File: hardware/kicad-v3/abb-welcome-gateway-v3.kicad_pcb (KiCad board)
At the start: 2 copper layers, 45.3 x 56.3 mm, 69 parts, among them P1 WJ500V-5.08-2P, Q1 S8050, Q2 S8050, Q3 S8050, Q4 2N7002, Q5 2N7002, Q6 2N7002, SW1 TS-1187A-B-A-B, U1 TPS5430DDAR, U2 ESP32-S3-WROOM-1-N16R8, U3 74LVC1G14

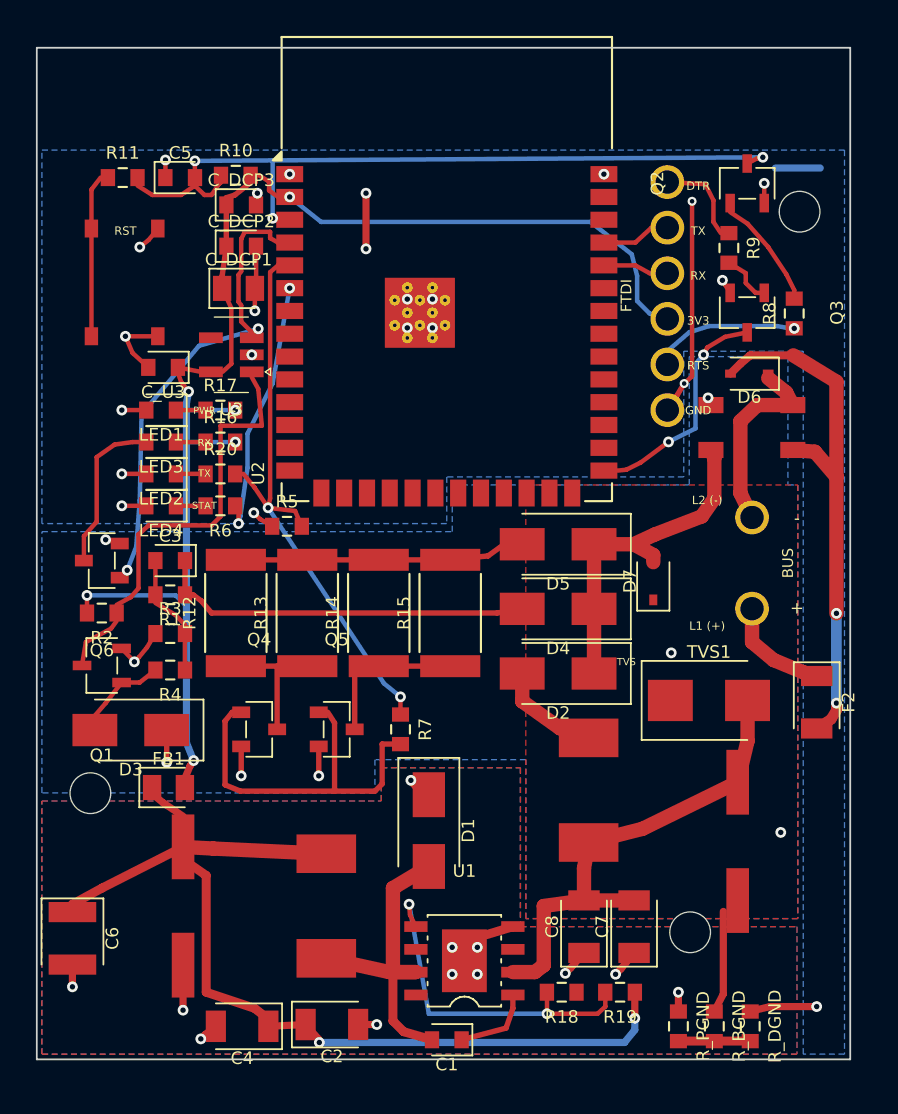
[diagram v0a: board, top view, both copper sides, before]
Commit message: PCB v3: serigrafia — refs dentro del borde + autor y fecha
- Reubicadas al interior las referencias que se salian del contorno:
  C1/C2/C4 y las tres 0R del star point (R_PGND/R_BGND/R_DGND) al norte de
  su componente; R10/R11/C5 fuera de la franja de antena; F2/Q3 hacia dentro.
  Verificado: 0 referencias fuera del borde.
- Anadido en la cara inferior (B.SilkS): github.com/fquinto y nov-2026,
  bajo el titulo existente.
- DRC electrico intacto (0 errores, 0 unconnected). Render top actualizado.
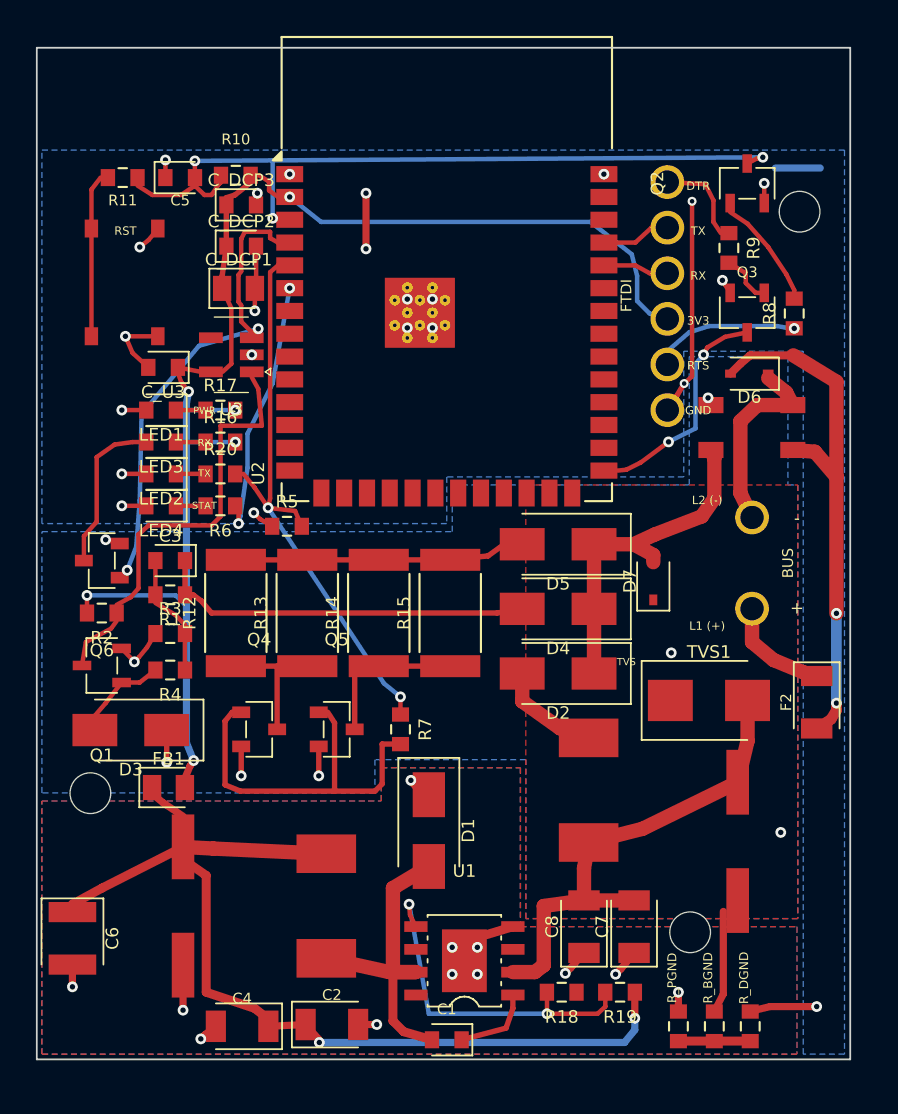
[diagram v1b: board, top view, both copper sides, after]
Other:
- board text added: "github.com/fquinto"
- board text added: "nov-2026"
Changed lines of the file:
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@@
 		(at 93.6 129.199999)
 		(property "Reference" "C2"
-			(at 0 1.775 0)
+			(at 0 -1.649999 0)
 			(layer "F.SilkS")
 			(effects
 				(font
-					(size 0.7 0.7)
-					(thickness 0.12)
+					(size 0.6 0.6)
+					(thickness 0.1)
 				)
 			)
@@
 		(at 88.6 129.3 180)
 		(property "Reference" "C4"
-			(at 0 -1.775 180)
+			(at 0 1.55 0)
 			(layer "F.SilkS")
 			(effects
 				(font
-					(size 0.7 0.7)
-					(thickness 0.12)
+					(size 0.6 0.6)
+					(thickness 0.1)
 				)
 			)
@@
 		(at 120.6 111.25 -90)
 		(property "Reference" "F2"
-			(at 0 -1.775 270)
+			(at 0 1.7 90)
 			(layer "F.SilkS")
 			(effects
 				(font
-					(size 0.7 0.7)
-					(thickness 0.12)
+					(size 0.6 0.6)
+					(thickness 0.1)
 				)
 			)
@@
 		(at 85.15 82.03)
 		(property "Reference" "C5"
-			(at 0 -1.375 0)
+			(at 0 1.27 0)
 			(layer "F.SilkS")
 			(effects
 				(font
-					(size 0.7 0.7)
-					(thickness 0.12)
+					(size 0.6 0.6)
+					(thickness 0.1)
 				)
 			)
@@
 		(at 81.95 82.03)
 		(property "Reference" "R11"
-			(at 0 -1.375 0)
+			(at 0 1.27 0)
 			(layer "F.SilkS")
 			(effects
 				(font
-					(size 0.7 0.7)
-					(thickness 0.12)
+					(size 0.6 0.6)
+					(thickness 0.1)
 				)
 			)
@@
 		(at 88.25 81.9)
 		(property "Reference" "R10"
-			(at 0 -1.375 0)
+			(at 0 -2 0)
 			(layer "F.SilkS")
 			(effects
 				(font
-					(size 0.7 0.7)
-					(thickness 0.12)
+					(size 0.6 0.6)
+					(thickness 0.1)
 				)
 			)
@@
 		(at 116.73 89.55 90)
 		(property "Reference" "Q3"
-			(at 0 5 90)
+			(at 2.25 0 0)
 			(layer "F.SilkS")
 			(effects
 				(font
-					(size 0.7 0.7)
-					(thickness 0.12)
+					(size 0.6 0.6)
+					(thickness 0.1)
 				)
 			)
@@
 		(at 114.9 129.3 -90)
 		(property "Reference" "R_BGND"
-			(at 0 -1.375 270)
+			(at -2.7 0.35 90)
 			(layer "F.SilkS")
 			(effects
 				(font
-					(size 0.7 0.7)
-					(thickness 0.12)
+					(size 0.5 0.5)
+					(thickness 0.1)
 				)
 			)
@@
 		(at 112.9 129.3 -90)
 		(property "Reference" "R_PGND"
-			(at 0 -1.375 270)
+			(at -2.7 0.35 90)
 			(layer "F.SilkS")
 			(effects
 				(font
-					(size 0.7 0.7)
-					(thickness 0.12)
+					(size 0.5 0.5)
+					(thickness 0.1)
 				)
 			)
@@
 		(at 116.9 129.3 -90)
 		(property "Reference" "R_DGND"
-			(at 0 -1.375 270)
+			(at -2.7 0.35 90)
 			(layer "F.SilkS")
 			(effects
 				(font
-					(size 0.7 0.7)
-					(thickness 0.12)
+					(size 0.5 0.5)
+					(thickness 0.1)
 				)
 			)
@@
 		(at 100 130.05 180)
 		(property "Reference" "C1"
-			(at 0 -1.375 180)
+			(at 0 1.7 0)
 			(layer "F.SilkS")
 			(effects
 				(font
-					(size 0.7 0.7)
-					(thickness 0.12)
+					(size 0.6 0.6)
+					(thickness 0.1)
 				)
 			)
@@
 			)
 			(justify mirror)
+		)
+	)
+	(gr_text "nov-2026"
+		(at 100 114.3 0)
+		(layer "B.SilkS")
+		(effects
+			(font
+				(size 1.1 1.1)
+				(thickness 0.2)
+			)
+			(justify mirror)
+		)
+	)
+	(gr_text "github.com/fquinto"
+		(at 100 112 0)
+		(layer "B.SilkS")
+		(effects
+			(font
+				(size 1.1 1.1)
+				(thickness 0.2)
+			)
+			(justify mirror)
